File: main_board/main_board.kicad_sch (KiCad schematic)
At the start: 57 parts, among them J1 USB4105-GF-A-060, J2 Conn_ARM_JTAG_SWD_10, Q3 NX3008PBK,215, U1 SSD1306, U2 ESP32-S2-SOLO, U3 TLV62568PDRLT, U4 MCP73832, U5 DW01, U6 8205A, U7 MAX17055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

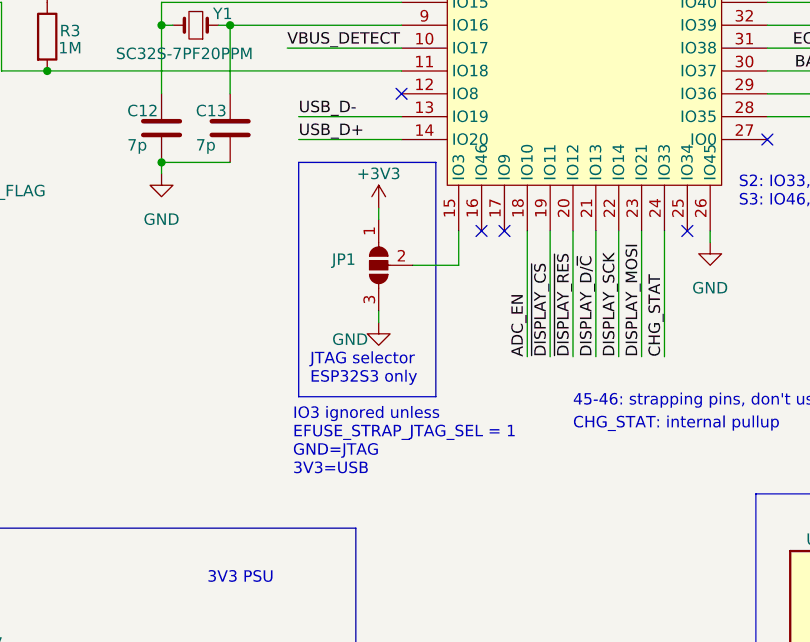
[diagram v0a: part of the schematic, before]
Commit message: Remove JTAG selector
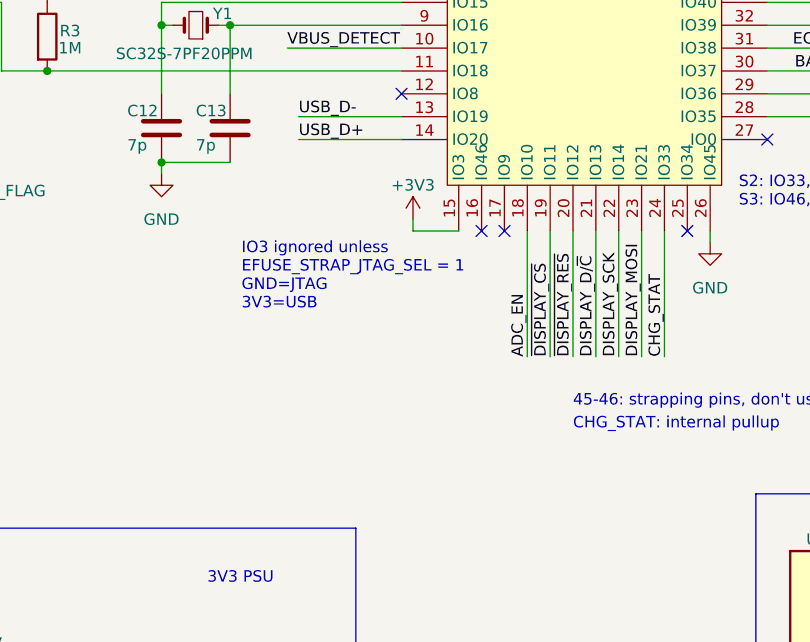
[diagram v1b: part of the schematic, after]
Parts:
- removed JP1: SolderJumper_3_Open, Jumper:SolderJumper-3_P1.3mm_Open_RoundedPad1.0x1.5mm, symbol Jumper:SolderJumper_3_Open
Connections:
- net +3V3: now also U2.15 (IO3)
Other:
- note removed: "JTAG selector ESP32S3 only"
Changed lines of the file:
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@@
-    (stroke (width 0) (type default))
-  )
-  (wire (pts (xy 135.89 78.74) (xy 135.89 82.55))
     (stroke (width 0) (type default))
   )
@@
     (stroke (width 0) (type default))
   )
-  (wire (pts (xy 127 87.63) (xy 127 88.9))
-    (stroke (width 0) (type default))
-  )
   (wire (pts (xy 120.65 139.7) (xy 115.57 139.7))
     (stroke (width 0) (type default))
@@
     (stroke (width 0) (type default))
   )
-  (wire (pts (xy 127 76.2) (xy 127 77.47))
+  (wire (pts (xy 130.81 77.47) (xy 130.81 78.74))
     (stroke (width 0) (type default))
   )
@@
     (stroke (width 0) (type default))
   )
-  (wire (pts (xy 135.89 82.55) (xy 130.81 82.55))
+  (wire (pts (xy 130.81 78.74) (xy 135.89 78.74))
     (stroke (width 0) (type default))
   )
@@
     (fill (type none))
   )
-  (rectangle (start 118.11 71.12) (end 133.35 97.155)
-    (stroke (width 0) (type default))
-    (fill (type none))
-  )
   (text "USB-C" (at 207.01 161.29 0)
     (effects (font (size 1.27 1.27)) (justify left bottom))
@@
   )
   (text "Fuel gauge" (at 140.97 160.655 0)
-    (effects (font (size 1.27 1.27)) (justify left bottom))
-  )
-  (text "JTAG selector\nESP32S3 only" (at 119.38 95.885 0)
     (effects (font (size 1.27 1.27)) (justify left bottom))
   )
@@
   )
   (text "IO3 ignored unless\nEFUSE_STRAP_JTAG_SEL = 1\nGND=JTAG\n3V3=USB"
-    (at 117.475 106.045 0)
+    (at 111.76 87.63 0)
     (effects (font (size 1.27 1.27)) (justify left bottom))
   )
@@
     )
   )
-  (symbol (lib_id "power:GND") (at 127 88.9 0) (unit 1)
-    (in_bom yes) (on_board yes) (dnp no)
-    (property "Reference" "#PWR040" (at 127 95.25 0)
-      (effects (font (size 1.27 1.27)) hide)
-    )
-    (property "Value" "GND" (at 123.825 90.805 0)
-      (effects (font (size 1.27 1.27)))
-    )
-    (property "Footprint" "" (at 127 88.9 0)
-      (effects (font (size 1.27 1.27)) hide)
-    )
-    (property "Datasheet" "" (at 127 88.9 0)
-      (effects (font (size 1.27 1.27)) hide)
-    )
-    (pin "1")
-    (instances
-      (project "main_board"
-        (path "/e55848cd-275a-4b5e-8e68-b5d8d07c8d31"
-          (reference "#PWR040") (unit 1)
-        )
-      )
-    )
-  )
   (symbol (lib_id "power:+BATT") (at 121.92 167.64 0) (mirror y) (unit 1)
     (in_bom yes) (on_board yes) (dnp no) (fields_autoplaced)
@@
     )
   )
-  (symbol (lib_id "power:+3V3") (at 127 76.2 0) (unit 1)
+  (symbol (lib_id "power:+3V3") (at 130.81 77.47 0) (unit 1)
     (in_bom yes) (on_board yes) (dnp no) (fields_autoplaced)
-    (property "Reference" "#PWR044" (at 127 80.01 0)
-      (effects (font (size 1.27 1.27)) hide)
-    )
-    (property "Value" "+3V3" (at 127 72.39 0)
-      (effects (font (size 1.27 1.27)))
-    )
-    (property "Footprint" "" (at 127 76.2 0)
-      (effects (font (size 1.27 1.27)) hide)
-    )
-    (property "Datasheet" "" (at 127 76.2 0)
+    (property "Reference" "#PWR044" (at 130.81 81.28 0)
+      (effects (font (size 1.27 1.27)) hide)
+    )
+    (property "Value" "+3V3" (at 130.81 73.66 0)
+      (effects (font (size 1.27 1.27)))
+    )
+    (property "Footprint" "" (at 130.81 77.47 0)
+      (effects (font (size 1.27 1.27)) hide)
+    )
+    (property "Datasheet" "" (at 130.81 77.47 0)
       (effects (font (size 1.27 1.27)) hide)
     )
@@
         )
       )
-    )
-  )
-  (symbol (lib_id "Jumper:SolderJumper_3_Open") (at 127 82.55 90) (mirror x) (unit 1)
-    (in_bom no) (on_board yes) (dnp no)
-    (property "Reference" "JP1" (at 124.46 81.915 90)
-      (effects (font (size 1.27 1.27)) (justify left))
-    )
-    (property "Value" "SolderJumper_3_Open" (at 124.46 80.645 90)
-      (effects (font (size 1.27 1.27)) (justify left) hide)
-    )
-    (property "Footprint" "Jumper:SolderJumper-3_P1.3mm_Open_RoundedPad1.0x1.5mm" (at 127 82.55 0)
-      (effects (font (size 1.27 1.27)) hide)
-    )
-    (property "Datasheet" "~" (at 127 82.55 0)
-      (effects (font (size 1.27 1.27)) hide)
-    )
-    (pin "1")
-    (pin "2")
-    (pin "3")
-    (instances
-      (project "main_board"
-        (path "/e55848cd-275a-4b5e-8e68-b5d8d07c8d31"
-          (reference "JP1") (unit 1)
-        )
-      )

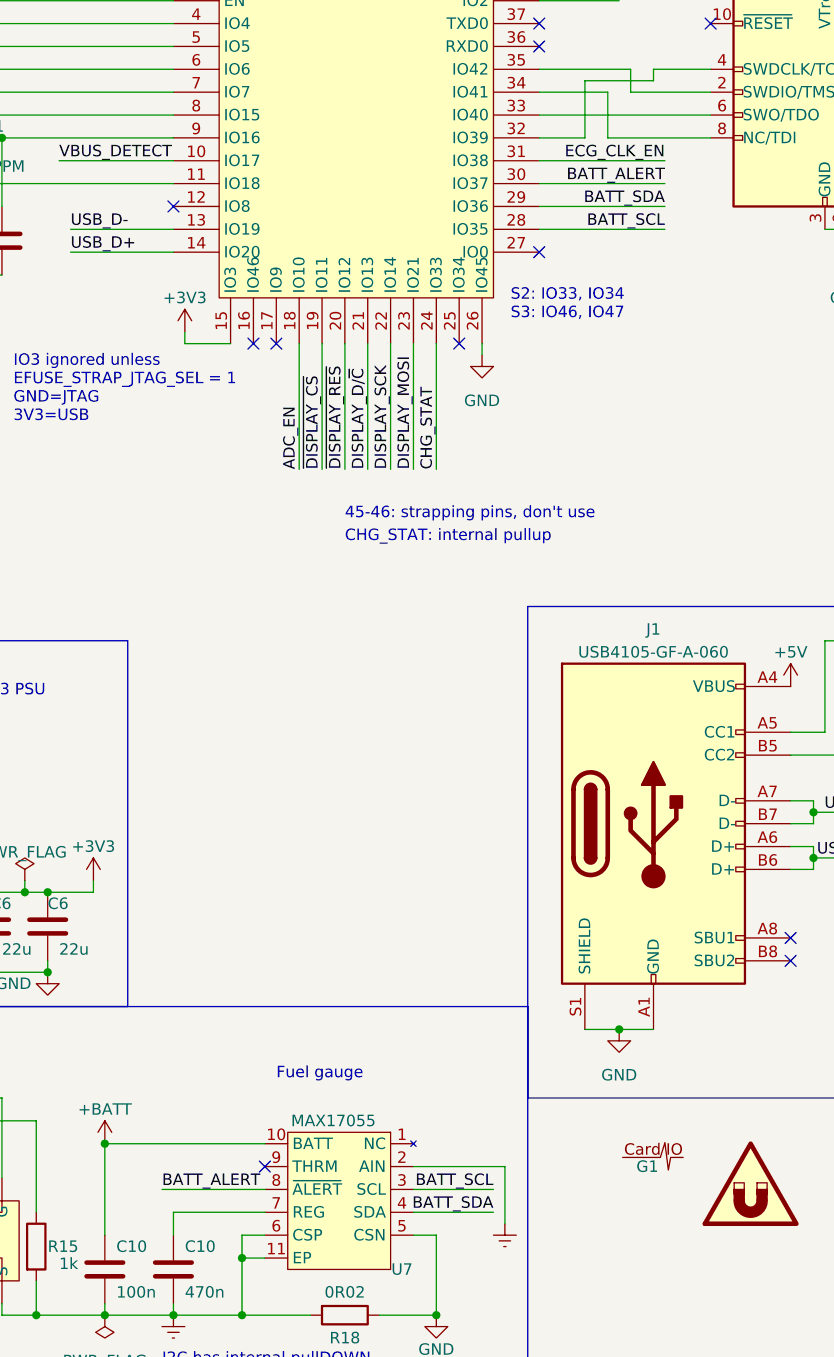
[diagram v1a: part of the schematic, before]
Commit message: Replace battery alert input with ADC_EN
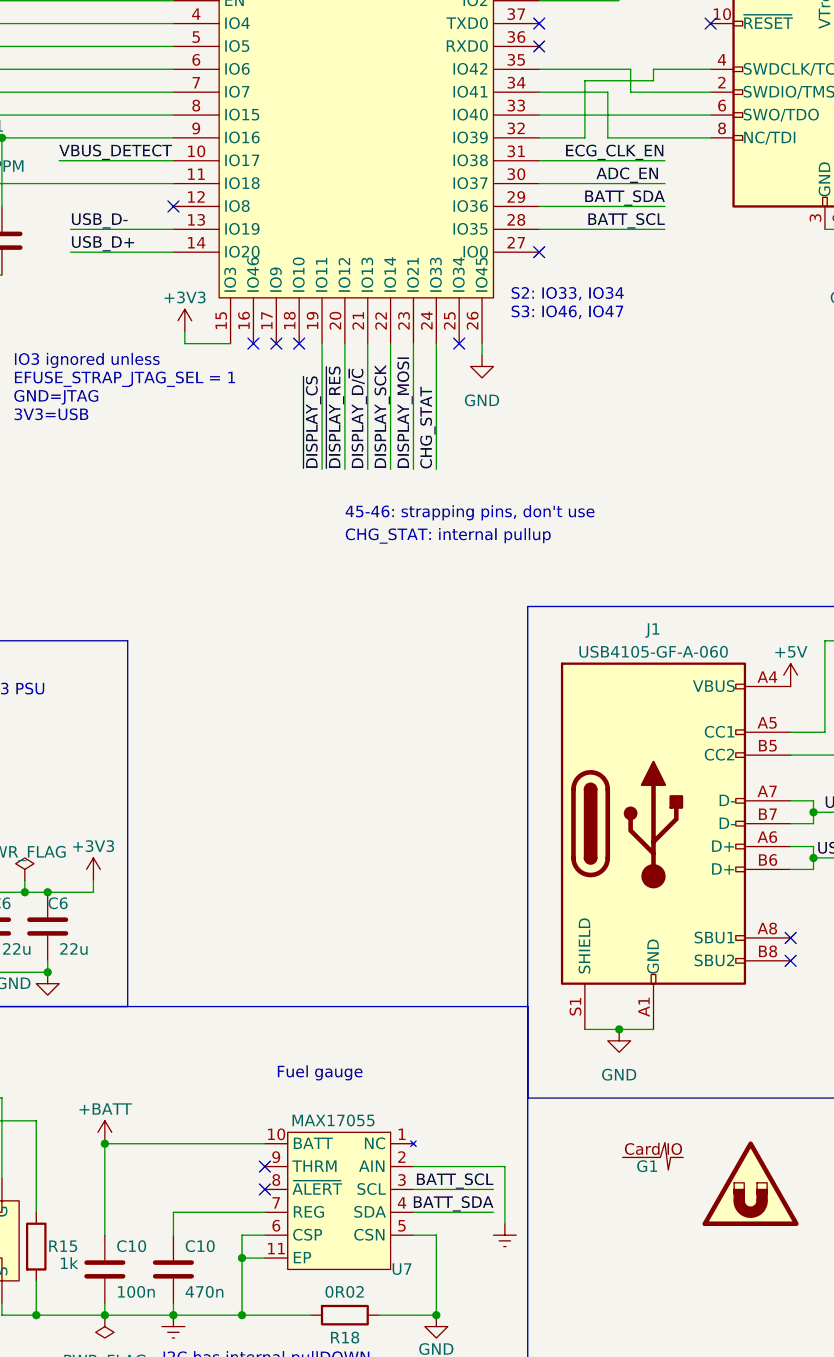
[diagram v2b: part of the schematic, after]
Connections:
- net ADC_EN: now also U2.30 (IO37); no longer U2.18 (IO10)
- net BATT_ALERT: no longer names the net of U7.8 (~{ALERT})
- net BATT_ALERT: no longer U2.30 (IO37)
- no-connect marks 13 -> 15
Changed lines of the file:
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@@
   (no_connect (at 170.18 43.18))
   (no_connect (at 139.7 170.18))
+  (no_connect (at 170.18 68.58))
+  (no_connect (at 143.51 78.74))
   (no_connect (at 161.29 78.74))
-  (no_connect (at 170.18 68.58))
+  (no_connect (at 139.7 172.72))
   (no_connect (at 140.97 78.74))
   (no_connect (at 198.12 147.32))
@@
     (stroke (width 0) (type default))
   )
-  (wire (pts (xy 128.27 172.72) (xy 139.7 172.72))
-    (stroke (width 0) (type default))
-  )
   (wire (pts (xy 43.18 194.31) (xy 43.18 190.5))
     (stroke (width 0) (type default))
@@
   )
   (wire (pts (xy 128.27 27.94) (xy 121.92 27.94))
-    (stroke (width 0) (type default))
-  )
-  (wire (pts (xy 143.51 78.74) (xy 143.51 92.71))
     (stroke (width 0) (type default))
   )
@@
     (effects (font (size 1.27 1.27)) (justify left bottom))
   )
-  (label "ADC_EN" (at 143.51 92.71 90) (fields_autoplaced)
+  (label "ADC_EN" (at 176.53 60.96 0) (fields_autoplaced)
     (effects (font (size 1.27 1.27)) (justify left bottom))
   )
@@
     (effects (font (size 1.27 1.27)) (justify right bottom))
   )
-  (label "BATT_ALERT" (at 184.15 60.96 180) (fields_autoplaced)
-    (effects (font (size 1.27 1.27)) (justify right bottom))
-  )
   (label "BATT_SDA" (at 165.1 175.26 180) (fields_autoplaced)
     (effects (font (size 1.27 1.27)) (justify right bottom))
@@
     (effects (font (size 1.27 1.27)) (justify right bottom))
   )
-  (label "BATT_ALERT" (at 128.27 172.72 0) (fields_autoplaced)
-    (effects (font (size 1.27 1.27)) (justify left bottom))
-  )
   (label "~{DISPLAY_CS}" (at 146.05 92.71 90) (fields_autoplaced)

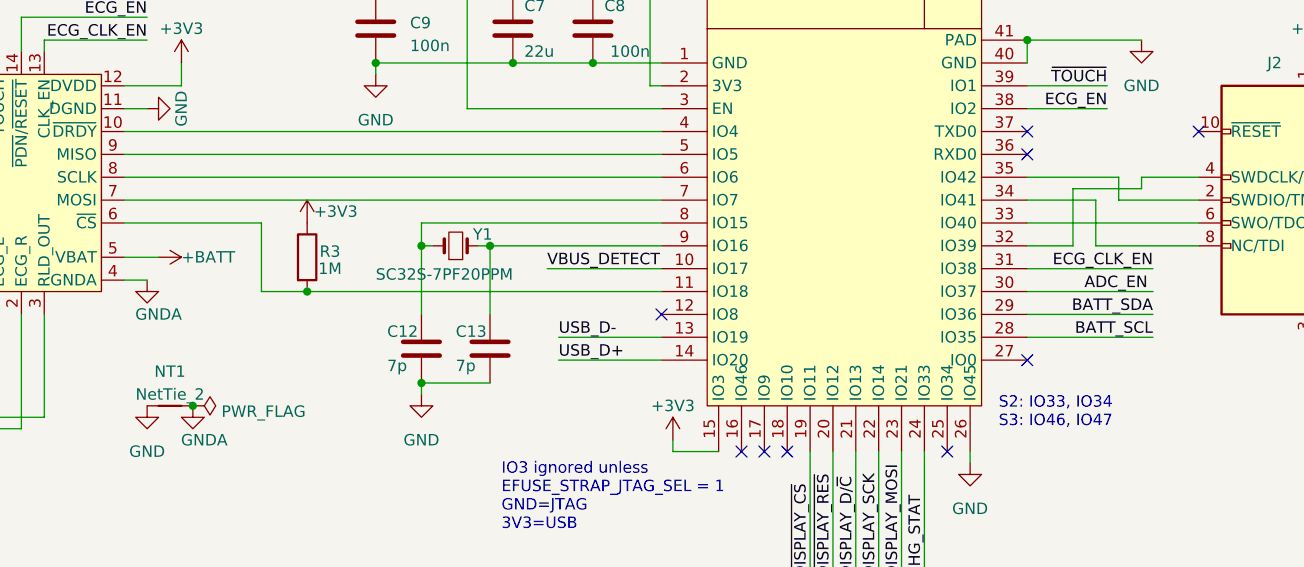
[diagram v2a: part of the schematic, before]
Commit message: Move frontend chip select to IO0
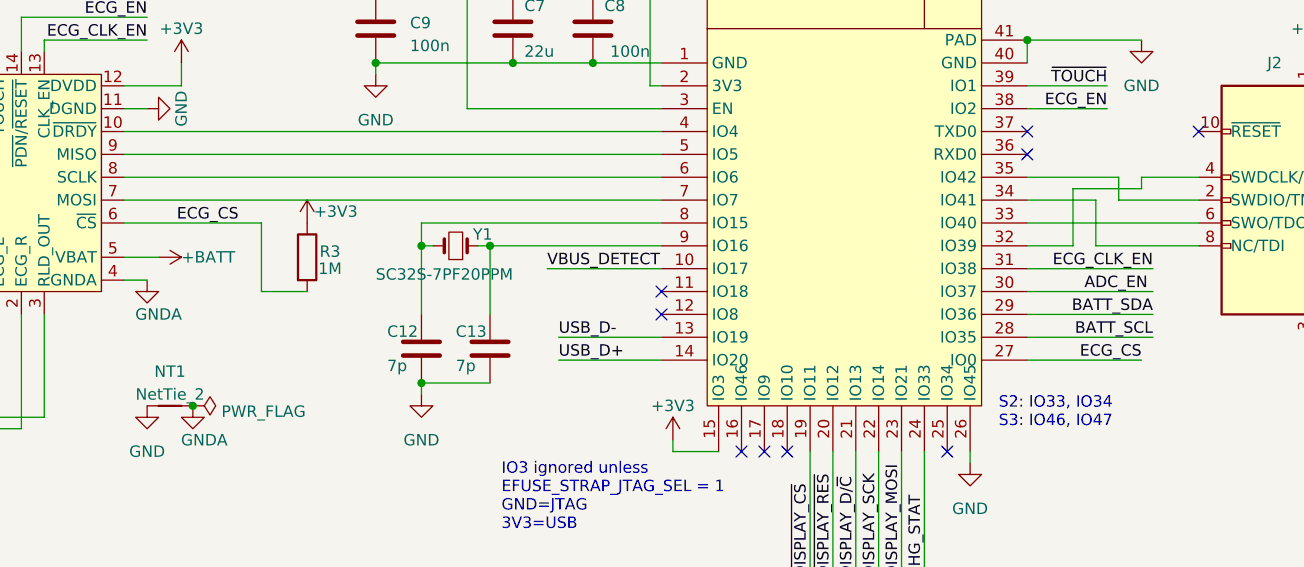
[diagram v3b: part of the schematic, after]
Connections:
- net ECG_CS: now reaches M1.6 (~{CS}), R3.2
- net ECG_CS: now also U2.27 (IO0); no longer U2.11 (IO18)
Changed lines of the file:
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@@
   (junction (at 44.45 134.62) (diameter 0) (color 0 0 0 0)
-  )
-  (junction (at 90.17 60.96) (diameter 0) (color 0 0 0 0)
   )
   (junction (at 74.93 172.72) (diameter 0) (color 0 0 0 0)
@@
   (no_connect (at 129.54 63.5))
   (no_connect (at 254 109.22))
+  (no_connect (at 129.54 60.96))
   (no_connect (at 138.43 78.74))
   (no_connect (at 170.18 45.72))
@@
   (no_connect (at 170.18 43.18))
   (no_connect (at 139.7 170.18))
-  (no_connect (at 170.18 68.58))
   (no_connect (at 143.51 78.74))
   (no_connect (at 161.29 78.74))
@@
     (stroke (width 0) (type default))
   )
-  (wire (pts (xy 90.17 60.96) (xy 129.54 60.96))
-    (stroke (width 0) (type default))
-  )
   (wire (pts (xy 95.25 186.69) (xy 95.25 185.42))
     (stroke (width 0) (type default))
@@
   )
   (wire (pts (xy 240.03 48.26) (xy 240.03 52.07))
+    (stroke (width 0) (type default))
+  )
+  (wire (pts (xy 170.18 68.58) (xy 182.88 68.58))
     (stroke (width 0) (type default))
   )
@@
     (effects (font (size 1.27 1.27)) (justify left bottom))
   )
+  (label "ECG_CS" (at 82.55 53.34 180) (fields_autoplaced)
+    (effects (font (size 1.27 1.27)) (justify right bottom))
+  )
   (label "~{DISPLAY_RES}" (at 228.6 86.36 0) (fields_autoplaced)
     (effects (font (size 1.27 1.27)) (justify left bottom))
@@
     (effects (font (size 1.27 1.27)) (justify left bottom))
   )
+  (label "ECG_CS" (at 182.88 68.58 180) (fields_autoplaced)
+    (effects (font (size 1.27 1.27)) (justify right bottom))
+  )
   (label "BATT_SCL" (at 165.1 172.72 180) (fields_autoplaced)

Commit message: Merge ECG_EN and ADC_EN
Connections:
- net ECG_EN is gone; now on net ANALOG_EN: M1.14 (~{PDN}/~{RESET}), U2.38 (IO2)
- net ~{DISPLAY_CS}: now also U2.12 (IO8); no longer U2.19 (IO11)
- net ~{DISPLAY_RES}: now also U2.11 (IO18); no longer U2.20 (IO12)
- net ADC_EN renamed ANALOG_EN
- net ANALOG_EN: no longer U2.30 (IO37)
- no-connect marks 15 -> 16
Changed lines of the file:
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@@
   (junction (at 102.87 55.88) (diameter 0) (color 0 0 0 0)
   )
-  (no_connect (at 129.54 63.5))
   (no_connect (at 254 109.22))
-  (no_connect (at 129.54 60.96))
   (no_connect (at 138.43 78.74))
+  (no_connect (at 170.18 60.96))
   (no_connect (at 170.18 45.72))
   (no_connect (at 189.23 43.18))
   (no_connect (at 198.12 144.78))
+  (no_connect (at 148.59 78.74))
   (no_connect (at 170.18 43.18))
   (no_connect (at 139.7 170.18))
@@
   (no_connect (at 161.29 78.74))
   (no_connect (at 139.7 172.72))
+  (no_connect (at 146.05 78.74))
   (no_connect (at 140.97 78.74))
   (no_connect (at 198.12 147.32))
@@
     (stroke (width 0) (type default))
   )
-  (wire (pts (xy 146.05 78.74) (xy 146.05 92.71))
-    (stroke (width 0) (type default))
-  )
   (wire (pts (xy 110.49 162.56) (xy 110.49 171.45))
     (stroke (width 0) (type default))
@@
     (stroke (width 0) (type default))
   )
-  (wire (pts (xy 170.18 40.64) (xy 179.07 40.64))
+  (wire (pts (xy 170.18 40.64) (xy 181.61 40.64))
     (stroke (width 0) (type default))
   )
@@
     (stroke (width 0) (type default))
   )
+  (wire (pts (xy 116.84 60.96) (xy 129.54 60.96))
+    (stroke (width 0) (type default))
+  )
   (wire (pts (xy 121.92 186.69) (xy 121.92 185.42))
     (stroke (width 0) (type default))
@@
     (stroke (width 0) (type default))
   )
-  (wire (pts (xy 148.59 78.74) (xy 148.59 92.71))
-    (stroke (width 0) (type default))
-  )
   (wire (pts (xy 254 143.51) (xy 254 147.32))
     (stroke (width 0) (type default))
@@
     (stroke (width 0) (type default))
   )
-  (wire (pts (xy 184.15 60.96) (xy 170.18 60.96))
-    (stroke (width 0) (type default))
-  )
   (wire (pts (xy 120.65 138.43) (xy 120.65 139.7))
     (stroke (width 0) (type default))
   )
   (wire (pts (xy 102.87 53.34) (xy 129.54 53.34))
+    (stroke (width 0) (type default))
+  )
+  (wire (pts (xy 116.84 63.5) (xy 129.54 63.5))
     (stroke (width 0) (type default))
   )
@@
     (effects (font (size 1.27 1.27)) (justify left bottom))
   )
-  (label "ECG_EN" (at 179.07 40.64 180) (fields_autoplaced)
+  (label "ANALOG_EN" (at 181.61 40.64 180) (fields_autoplaced)
     (effects (font (size 1.27 1.27)) (justify right bottom))
   )
@@
     (effects (font (size 1.27 1.27)) (justify left bottom))
   )
+  (label "ANALOG_EN" (at 72.39 30.48 180) (fields_autoplaced)
+    (effects (font (size 1.27 1.27)) (justify right bottom))
+  )
   (label "ECG_CS" (at 182.88 68.58 180) (fields_autoplaced)
     (effects (font (size 1.27 1.27)) (justify right bottom))
@@
     (effects (font (size 1.27 1.27)) (justify right bottom))
   )
-  (label "ADC_EN" (at 36.83 182.88 0) (fields_autoplaced)
-    (effects (font (size 1.27 1.27)) (justify left bottom))
-  )
   (label "BATT_SDA" (at 25.4 194.31 0) (fields_autoplaced)
     (effects (font (size 1.27 1.27)) (justify left bottom))
@@
     (effects (font (size 1.27 1.27)) (justify left bottom))
   )
-  (label "ADC_EN" (at 176.53 60.96 0) (fields_autoplaced)
-    (effects (font (size 1.27 1.27)) (justify left bottom))
-  )
   (label "CHG_STAT" (at 158.75 92.71 90) (fields_autoplaced)
     (effects (font (size 1.27 1.27)) (justify left bottom))
@@
     (effects (font (size 1.27 1.27)) (justify left bottom))
   )
+  (label "ANALOG_EN" (at 43.18 182.88 180) (fields_autoplaced)
+    (effects (font (size 1.27 1.27)) (justify right bottom))
+  )
   (label "BATT_SCL" (at 184.15 66.04 180) (fields_autoplaced)
     (effects (font (size 1.27 1.27)) (justify right bottom))
@@
     (effects (font (size 1.27 1.27)) (justify right bottom))
   )
-  (label "~{DISPLAY_CS}" (at 146.05 92.71 90) (fields_autoplaced)
-    (effects (font (size 1.27 1.27)) (justify left bottom))
-  )
-  (label "ECG_EN" (at 72.39 30.48 180) (fields_autoplaced)
-    (effects (font (size 1.27 1.27)) (justify right bottom))
+  (label "~{DISPLAY_CS}" (at 116.84 63.5 0) (fields_autoplaced)
+    (effects (font (size 1.27 1.27)) (justify left bottom))
   )
   (label "ECG_CLK_EN" (at 184.15 58.42 180) (fields_autoplaced)
     (effects (font (size 1.27 1.27)) (justify right bottom))
   )
-  (label "~{DISPLAY_RES}" (at 148.59 92.71 90) (fields_autoplaced)
-    (effects (font (size 1.27 1.27)) (justify left bottom))
-  )
+  (label "~{DISPLAY_RES}" (at 116.84 60.96 0) (fields_autoplaced)
+    (effects (font (size 1.27 1.27)) (justify left bottom))
+  )
